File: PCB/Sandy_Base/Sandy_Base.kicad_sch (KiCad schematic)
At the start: 169 parts, among them J1 Conn_02x02_Top_Bottom, J10 Conn_01x03, J2 Conn_02x02_Top_Bottom, J3 Conn_02x02_Top_Bottom, J4 Conn_02x02_Top_Bottom, J5 Conn_02x02_Top_Bottom, J6 Conn_02x02_Top_Bottom, J7 USB_C_Receptacle_USB2.0, J8 Conn_02x03_Odd_Even, J9 Conn_01x02, U1 ATmega32U4-MU, U2 24LC64, Y1 16MHz

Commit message: ひととおりのソケットへの変更完了（プレートまだない）
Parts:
- SW_LSFT1u2: footprint MX_Alps_Hybrid:MXOnly-1U-Hotswap-guide -> MX_Alps_Hybrid:MXOnly-1U-Hotswap-custom5-guide
- SW_LSFT2u1: footprint MX_Alps_Hybrid:MXOnly-2U-Hotswap-ReversedStabilizers-guide2 -> MX_Alps_Hybrid:MXOnly-2U-Hotswap-ReversedStabilizers-guide2-custom11
- SW_RSPC1.5u1: footprint MX_Alps_Hybrid:MXOnly-1.5U-Hotswap-guide -> MX_Alps_Hybrid:MXOnly-1.5U-Hotswap-custom11-guide
- SW_RSPC2u1: footprint MX_Alps_Hybrid:MXOnly-2U-Hotswap-guide2 -> MX_Alps_Hybrid:MXOnly-2U-Hotswap-custom1-guide2
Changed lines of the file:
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@@
       (effects (font (size 1.27 1.27)))
     )
-    (property "Footprint" "MX_Alps_Hybrid:MXOnly-2U-Hotswap-guide2" (at 177.8 172.72 0)
+    (property "Footprint" "MX_Alps_Hybrid:MXOnly-2U-Hotswap-custom1-guide2" (at 177.8 172.72 0)
       (effects (font (size 1.27 1.27)) hide)
     )
@@
       (effects (font (size 1.27 1.27)))
     )
-    (property "Footprint" "MX_Alps_Hybrid:MXOnly-2U-Hotswap-ReversedStabilizers-guide2" (at 29.21 140.97 0)
+    (property "Footprint" "MX_Alps_Hybrid:MXOnly-2U-Hotswap-ReversedStabilizers-guide2-custom11" (at 29.21 140.97 0)
       (effects (font (size 1.27 1.27)) hide)
     )
@@
       (effects (font (size 1.27 1.27)))
     )
-    (property "Footprint" "MX_Alps_Hybrid:MXOnly-1U-Hotswap-guide" (at 45.72 140.97 0)
+    (property "Footprint" "MX_Alps_Hybrid:MXOnly-1U-Hotswap-custom5-guide" (at 45.72 140.97 0)
       (effects (font (size 1.27 1.27)) hide)
     )
@@
       (effects (font (size 1.27 1.27)))
     )
-    (property "Footprint" "MX_Alps_Hybrid:MXOnly-1.5U-Hotswap-guide" (at 177.8 167.64 0)
+    (property "Footprint" "MX_Alps_Hybrid:MXOnly-1.5U-Hotswap-custom11-guide" (at 177.8 167.64 0)
       (effects (font (size 1.27 1.27)) hide)
     )

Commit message: 微調整
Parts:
- LOGO1: footprint Jones.local:Sandy_logo_w60 -> Jones.local:Sandy_logo_w60_new
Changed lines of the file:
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@@
       (effects (font (size 1.27 1.27)) (justify left))
     )
-    (property "Footprint" "Jones.local:Sandy_logo_w60" (at 223.52 211.455 0)
+    (property "Footprint" "Jones.local:Sandy_logo_w60_new" (at 223.52 211.455 0)
       (effects (font (size 1.27 1.27)) hide)
     )

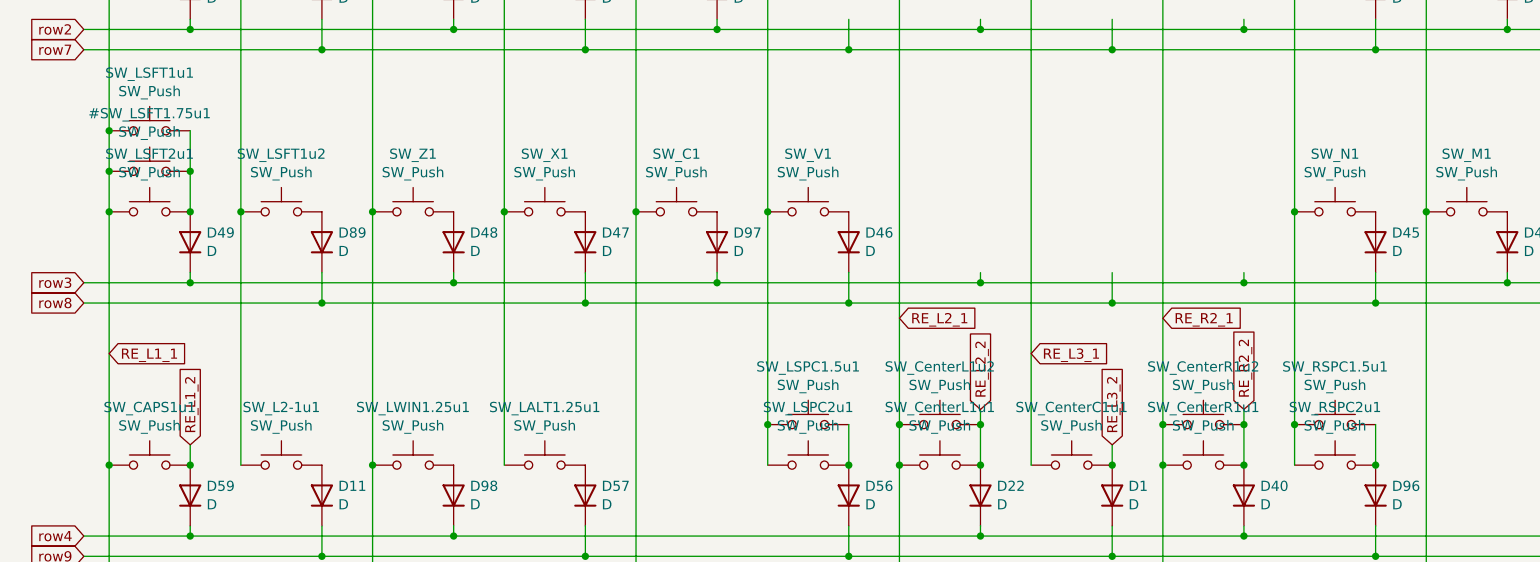
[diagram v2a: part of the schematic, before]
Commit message: 単一レイアウトに変更
最下行：5キー版のみ
左シフト：2uなし、1+1のみ
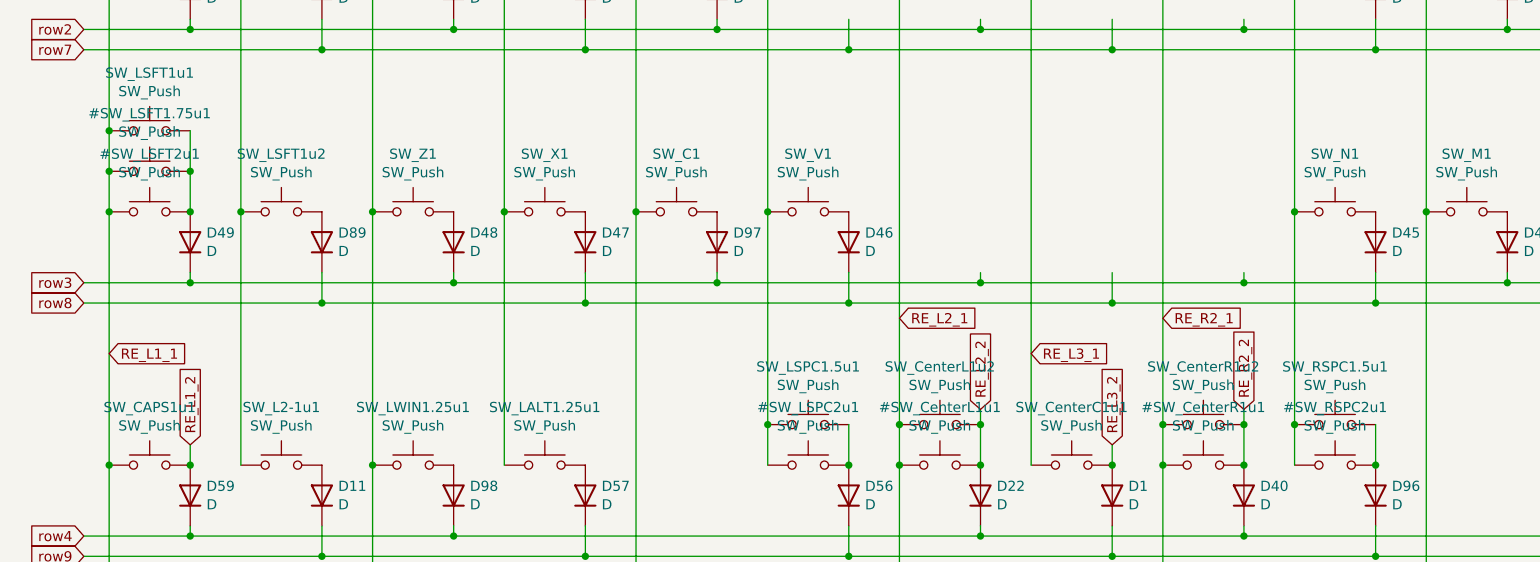
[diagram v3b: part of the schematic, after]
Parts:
- SW_CenterC1u1: footprint MX_Alps_Hybrid:MXOnly-1U-Hotswap-custom4-guide -> MX_Alps_Hybrid:MXOnly-1U-Hotswap-on-RE-guide
- SW_CenterL1u2: footprint MX_Alps_Hybrid:MXOnly-1U-Hotswap-custom2-guide -> MX_Alps_Hybrid:MXOnly-1U-Hotswap-guide
- SW_CenterR1u2: footprint MX_Alps_Hybrid:MXOnly-1U-Hotswap-custom3-guide -> MX_Alps_Hybrid:MXOnly-1U-Hotswap-guide
- SW_LSFT1u2: footprint MX_Alps_Hybrid:MXOnly-1U-Hotswap-custom5-guide -> MX_Alps_Hybrid:MXOnly-1U-Hotswap-guide
- SW_RSPC1.5u1: footprint MX_Alps_Hybrid:MXOnly-1.5U-Hotswap-custom11-guide -> MX_Alps_Hybrid:MXOnly-1.5U-Hotswap-guide
- renumbered SW_CenterL1u1 to #SW_CenterL1u1, SW_CenterR1u1 to #SW_CenterR1u1, SW_LSFT2u1 to #SW_LSFT2u1, SW_LSPC2u1 to #SW_LSPC2u1, SW_RSPC2u1 to #SW_RSPC2u1
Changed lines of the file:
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@@
   (symbol (lib_id "Switch:SW_Push") (at 177.8 177.8 0) (unit 1)
     (in_bom yes) (on_board yes) (dnp no)
-    (property "Reference" "SW_RSPC2u1" (at 177.8 170.561 0)
+    (property "Reference" "#SW_RSPC2u1" (at 177.8 170.561 0)
       (effects (font (size 1.27 1.27)))
     )
@@
       (project "Sandy_Base"
         (path "/a99ab643-cdc7-4f8c-8088-c1f4faa914d1"
-          (reference "SW_RSPC2u1") (unit 1)
+          (reference "#SW_RSPC2u1") (unit 1)
         )
       )
@@
   (symbol (lib_id "Switch:SW_Push") (at 29.21 146.05 0) (unit 1)
     (in_bom yes) (on_board yes) (dnp no)
-    (property "Reference" "SW_LSFT2u1" (at 29.21 138.811 0)
+    (property "Reference" "#SW_LSFT2u1" (at 29.21 138.811 0)
       (effects (font (size 1.27 1.27)))
     )
@@
       (project "Sandy_Base"
         (path "/a99ab643-cdc7-4f8c-8088-c1f4faa914d1"
-          (reference "SW_LSFT2u1") (unit 1)
+          (reference "#SW_LSFT2u1") (unit 1)
         )
       )
@@
   (symbol (lib_id "Switch:SW_Push") (at 111.76 177.8 0) (unit 1)
     (in_bom yes) (on_board yes) (dnp no)
-    (property "Reference" "SW_LSPC2u1" (at 111.76 170.561 0)
+    (property "Reference" "#SW_LSPC2u1" (at 111.76 170.561 0)
       (effects (font (size 1.27 1.27)))
     )
@@
       (project "Sandy_Base"
         (path "/a99ab643-cdc7-4f8c-8088-c1f4faa914d1"
-          (reference "SW_LSPC2u1") (unit 1)
+          (reference "#SW_LSPC2u1") (unit 1)
         )
       )
@@
       (effects (font (size 1.27 1.27)))
     )
-    (property "Footprint" "MX_Alps_Hybrid:MXOnly-1U-Hotswap-custom5-guide" (at 45.72 140.97 0)
+    (property "Footprint" "MX_Alps_Hybrid:MXOnly-1U-Hotswap-guide" (at 45.72 140.97 0)
       (effects (font (size 1.27 1.27)) hide)
     )
@@
   (symbol (lib_id "Switch:SW_Push") (at 128.27 177.8 0) (unit 1)
     (in_bom yes) (on_board yes) (dnp no)
-    (property "Reference" "SW_CenterL1u1" (at 128.27 170.561 0)
+    (property "Reference" "#SW_CenterL1u1" (at 128.27 170.561 0)
       (effects (font (size 1.27 1.27)))
     )
@@
       (project "Sandy_Base"
         (path "/a99ab643-cdc7-4f8c-8088-c1f4faa914d1"
-          (reference "SW_CenterL1u1") (unit 1)
+          (reference "#SW_CenterL1u1") (unit 1)
         )
       )
@@
   (symbol (lib_id "Switch:SW_Push") (at 161.29 177.8 0) (unit 1)
     (in_bom yes) (on_board yes) (dnp no)
-    (property "Reference" "SW_CenterR1u1" (at 161.29 170.561 0)
+    (property "Reference" "#SW_CenterR1u1" (at 161.29 170.561 0)
       (effects (font (size 1.27 1.27)))
     )
@@
       (project "Sandy_Base"
         (path "/a99ab643-cdc7-4f8c-8088-c1f4faa914d1"
-          (reference "SW_CenterR1u1") (unit 1)
+          (reference "#SW_CenterR1u1") (unit 1)
         )
       )
@@
       (effects (font (size 1.27 1.27)))
     )
-    (property "Footprint" "MX_Alps_Hybrid:MXOnly-1U-Hotswap-custom4-guide" (at 144.78 172.72 0)
+    (property "Footprint" "MX_Alps_Hybrid:MXOnly-1U-Hotswap-on-RE-guide" (at 144.78 172.72 0)
       (effects (font (size 1.27 1.27)) hide)
     )
@@
       (effects (font (size 1.27 1.27)))
     )
-    (property "Footprint" "MX_Alps_Hybrid:MXOnly-1U-Hotswap-custom2-guide" (at 128.27 167.64 0)
+    (property "Footprint" "MX_Alps_Hybrid:MXOnly-1U-Hotswap-guide" (at 128.27 167.64 0)
       (effects (font (size 1.27 1.27)) hide)
     )
@@
       (effects (font (size 1.27 1.27)))
     )
-    (property "Footprint" "MX_Alps_Hybrid:MXOnly-1.5U-Hotswap-custom11-guide" (at 177.8 167.64 0)
+    (property "Footprint" "MX_Alps_Hybrid:MXOnly-1.5U-Hotswap-guide" (at 177.8 167.64 0)
       (effects (font (size 1.27 1.27)) hide)
     )
@@
       (effects (font (size 1.27 1.27)))
     )
-    (property "Footprint" "MX_Alps_Hybrid:MXOnly-1U-Hotswap-custom3-guide" (at 161.29 167.64 0)
+    (property "Footprint" "MX_Alps_Hybrid:MXOnly-1U-Hotswap-guide" (at 161.29 167.64 0)
       (effects (font (size 1.27 1.27)) hide)
     )

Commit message: タブそのままで実用OKと判断し、LEDディフューザータブに繋がるネジ穴を削除
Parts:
- removed H90, H91: MountingHole, locallib:MountingHole_2.2mm_M2_No_Cu, symbol Mechanical:MountingHole
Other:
- note removed: "SCREWS to Diffuser"
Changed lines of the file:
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@@
     (effects (font (size 2.54 2.54) (thickness 0.508) bold) (justify left bottom))
   )
-  (text "SCREWS\nto Diffuser" (at 285.115 174.625 0)
-    (effects (font (size 2.54 2.54) (thickness 0.508) bold) (justify left bottom))
-  )
   (text "Virtual Connection" (at 140.335 284.48 0)
     (effects (font (size 1.27 1.27)) (justify left bottom))
@@
     )
   )
-  (symbol (lib_id "Mechanical:MountingHole") (at 292.1 182.88 0) (unit 1)
-    (in_bom yes) (on_board yes) (dnp no)
-    (property "Reference" "H91" (at 294.64 181.7116 0)
-      (effects (font (size 1.27 1.27)) (justify left))
-    )
-    (property "Value" "MountingHole" (at 294.64 184.023 0)
-      (effects (font (size 1.27 1.27)) (justify left))
-    )
-    (property "Footprint" "locallib:MountingHole_2.2mm_M2_No_Cu" (at 292.1 182.88 0)
-      (effects (font (size 1.27 1.27)) hide)
-    )
-    (property "Datasheet" "~" (at 292.1 182.88 0)
-      (effects (font (size 1.27 1.27)) hide)
-    )
-    (instances
-      (project "Sandy_Base"
-        (path "/a99ab643-cdc7-4f8c-8088-c1f4faa914d1"
-          (reference "H91") (unit 1)
-        )
-      )
-    )
-  )
   (symbol (lib_id "power:GND") (at 209.55 283.845 0) (unit 1)
     (in_bom yes) (on_board yes) (dnp no)
@@
         )
       )
-    )
-  )
-  (symbol (lib_id "Mechanical:MountingHole") (at 292.1 177.8 0) (unit 1)
-    (in_bom yes) (on_board yes) (dnp no)
-    (property "Reference" "H90" (at 294.64 176.6316 0)
-      (effects (font (size 1.27 1.27)) (justify left))
-    )
-    (property "Value" "MountingHole" (at 294.64 178.943 0)
-      (effects (font (size 1.27 1.27)) (justify left))
-    )
-    (property "Footprint" "locallib:MountingHole_2.2mm_M2_No_Cu" (at 292.1 177.8 0)
-      (effects (font (size 1.27 1.27)) hide)
-    )
-    (property "Datasheet" "~" (at 292.1 177.8 0)
-      (effects (font (size 1.27 1.27)) hide)
-    )
-    (instances
-      (project "Sandy_Base"
-        (path "/a99ab643-cdc7-4f8c-8088-c1f4faa914d1"
-          (reference "H90") (unit 1)
-        )
-      )

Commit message: 変更：USBコネクタをHRO TYPE-C-31-M-12に変更しSMTAに対応させる
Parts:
- J7: footprint Connector_USB:USB_C_Receptacle_GCT_USB4085 -> Connector_USB:USB_C_Receptacle_HRO_TYPE-C-31-M-12; LCSC (none) -> C165948
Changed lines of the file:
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@@
       (effects (font (size 1.27 1.27)))
     )
-    (property "Footprint" "Connector_USB:USB_C_Receptacle_GCT_USB4085" (at 334.01 167.64 0)
+    (property "Footprint" "Connector_USB:USB_C_Receptacle_HRO_TYPE-C-31-M-12" (at 334.01 167.64 0)
       (effects (font (size 1.27 1.27)) hide)
     )
@@
       (effects (font (size 1.27 1.27)) hide)
     )
+    (property "LCSC" "C165948" (at 330.2 167.64 0)
+      (effects (font (size 1.27 1.27)) hide)
+    )

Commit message: 変更：アクリル板を入れるための、パーツ移動
ダイオード、左端スイッチの上限反転、USBコネクタ周りのパーツを移動
Base基板の外形フットプリントで、右上ネジ穴にNPTHが残っていたのを除去。
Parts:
- D1: renamed from D28; footprint locallib:D_SOD-123_Emphasized_Direction_Line -> locallib:D_SOD-123_Emphasized_Direction_Line_Reference_on_bottom
- D10: renamed from D35; footprint locallib:D_SOD-123_Emphasized_Direction_Line -> locallib:D_SOD-123_Emphasized_Direction_Line_Reference_on_bottom
- D11: renamed from D34; footprint locallib:D_SOD-123_Emphasized_Direction_Line -> locallib:D_SOD-123_Emphasized_Direction_Line_Reference_on_bottom
- D12: renamed from D84; footprint locallib:D_SOD-123_Emphasized_Direction_Line -> locallib:D_SOD-123_Emphasized_Direction_Line_Reference_on_bottom
- D13: renamed from D44; footprint locallib:D_SOD-123_Emphasized_Direction_Line -> locallib:D_SOD-123_Emphasized_Direction_Line_Reference_on_bottom
- D14: renamed from D32; footprint locallib:D_SOD-123_Emphasized_Direction_Line -> locallib:D_SOD-123_Emphasized_Direction_Line_Reference_on_bottom
- D15: renamed from D49; footprint locallib:D_SOD-123_Emphasized_Direction_Line -> locallib:D_SOD-123_Emphasized_Direction_Line_Reference_on_bottom
- D16: renamed from D89; footprint locallib:D_SOD-123_Emphasized_Direction_Line -> locallib:D_SOD-123_Emphasized_Direction_Line_Reference_on_bottom
- D17: renamed from D48; footprint locallib:D_SOD-123_Emphasized_Direction_Line -> locallib:D_SOD-123_Emphasized_Direction_Line_Reference_on_bottom
- D18: renamed from D47; footprint locallib:D_SOD-123_Emphasized_Direction_Line -> locallib:D_SOD-123_Emphasized_Direction_Line_Reference_on_bottom
- D19: renamed from D97; footprint locallib:D_SOD-123_Emphasized_Direction_Line -> locallib:D_SOD-123_Emphasized_Direction_Line_Reference_on_bottom
- D2: renamed from D27; footprint locallib:D_SOD-123_Emphasized_Direction_Line -> locallib:D_SOD-123_Emphasized_Direction_Line_Reference_on_bottom
- D20: renamed from D46; footprint locallib:D_SOD-123_Emphasized_Direction_Line -> locallib:D_SOD-123_Emphasized_Direction_Line_Reference_on_bottom
- D21: renamed from D45; footprint locallib:D_SOD-123_Emphasized_Direction_Line -> locallib:D_SOD-123_Emphasized_Direction_Line_Reference_on_bottom
- D22: renamed from D43; footprint locallib:D_SOD-123_Emphasized_Direction_Line -> locallib:D_SOD-123_Emphasized_Direction_Line_Reference_on_bottom
- D23: renamed from D94; footprint locallib:D_SOD-123_Emphasized_Direction_Line -> locallib:D_SOD-123_Emphasized_Direction_Line_Reference_on_bottom
- D24: renamed from D93; footprint locallib:D_SOD-123_Emphasized_Direction_Line -> locallib:D_SOD-123_Emphasized_Direction_Line_Reference_on_bottom
- D25: renamed from D41; footprint locallib:D_SOD-123_Emphasized_Direction_Line -> locallib:D_SOD-123_Emphasized_Direction_Line_Reference_on_bottom
- D26: renamed from D91; footprint locallib:D_SOD-123_Emphasized_Direction_Line -> locallib:D_SOD-123_Emphasized_Direction_Line_Reference_on_bottom
- D27: renamed from D59; footprint locallib:D_SOD-123_Emphasized_Direction_Line -> locallib:D_SOD-123_Emphasized_Direction_Line_Reference_on_bottom
- D28: renamed from D11; footprint locallib:D_SOD-123_Emphasized_Direction_Line -> locallib:D_SOD-123_Emphasized_Direction_Line_Reference_on_bottom
- D29: renamed from D98; footprint locallib:D_SOD-123_Emphasized_Direction_Line -> locallib:D_SOD-123_Emphasized_Direction_Line_Reference_on_bottom
- D3: renamed from D24; footprint locallib:D_SOD-123_Emphasized_Direction_Line -> locallib:D_SOD-123_Emphasized_Direction_Line_Reference_on_bottom
- D30: renamed from D57; footprint locallib:D_SOD-123_Emphasized_Direction_Line -> locallib:D_SOD-123_Emphasized_Direction_Line_Reference_on_bottom
- D31: renamed from D56; footprint locallib:D_SOD-123_Emphasized_Direction_Line -> locallib:D_SOD-123_Emphasized_Direction_Line_Reference_on_bottom
- D32: renamed from D22; footprint locallib:D_SOD-123_Emphasized_Direction_Line -> locallib:D_SOD-123_Emphasized_Direction_Line_Reference_on_bottom
- D33: renamed from D1; footprint locallib:D_SOD-123_Emphasized_Direction_Line -> locallib:D_SOD-123_Emphasized_Direction_Line_Reference_on_bottom
- D34: renamed from D40; footprint locallib:D_SOD-123_Emphasized_Direction_Line -> locallib:D_SOD-123_Emphasized_Direction_Line_Reference_on_bottom
- D35: renamed from D96; footprint locallib:D_SOD-123_Emphasized_Direction_Line -> locallib:D_SOD-123_Emphasized_Direction_Line_Reference_on_bottom
- D36: renamed from D53; footprint locallib:D_SOD-123_Emphasized_Direction_Line -> locallib:D_SOD-123_Emphasized_Direction_Line_Reference_on_bottom
- D37: renamed from D92; footprint locallib:D_SOD-123_Emphasized_Direction_Line -> locallib:D_SOD-123_Emphasized_Direction_Line_Reference_on_bottom
- D38: renamed from D52; footprint locallib:D_SOD-123_Emphasized_Direction_Line -> locallib:D_SOD-123_Emphasized_Direction_Line_Reference_on_bottom
- D39: renamed from D51; footprint locallib:D_SOD-123_Emphasized_Direction_Line -> locallib:D_SOD-123_Emphasized_Direction_Line_Reference_on_bottom
- D4: renamed from D74; footprint locallib:D_SOD-123_Emphasized_Direction_Line -> locallib:D_SOD-123_Emphasized_Direction_Line_Reference_on_bottom
- D5: renamed from D39; footprint locallib:D_SOD-123_Emphasized_Direction_Line -> locallib:D_SOD-123_Emphasized_Direction_Line_Reference_on_bottom
- D6: renamed from D79; footprint locallib:D_SOD-123_Emphasized_Direction_Line -> locallib:D_SOD-123_Emphasized_Direction_Line_Reference_on_bottom
- D7: renamed from D38; footprint locallib:D_SOD-123_Emphasized_Direction_Line -> locallib:D_SOD-123_Emphasized_Direction_Line_Reference_on_bottom
- D8: renamed from D37; footprint locallib:D_SOD-123_Emphasized_Direction_Line -> locallib:D_SOD-123_Emphasized_Direction_Line_Reference_on_bottom
- D9: renamed from D87; footprint locallib:D_SOD-123_Emphasized_Direction_Line -> locallib:D_SOD-123_Emphasized_Direction_Line_Reference_on_bottom
- renumbered D10 to D99

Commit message: WIP:　アンダーグローLED #98
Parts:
- removed LED3, LED4: SK6812MINI, locallib:LED_SK6812MINI_PLCC4_3.5x3.5mm_P1.75mm_minimal, symbol LED:SK6812MINI
- added L1, L10, L11, L12, L13, L14, L15, L16, L2, L3, L4, L5, L6, L7, L8, L9: SK6812MINI-E, locallib:YS-SK6812MINI-E_middle_hole_with_small_pad, symbol kbd:SK6812MINI-E
- C1: footprint Capacitor_SMD:C_0805_2012Metric_Pad1.18x1.45mm_HandSolder -> locallib:YS-SK6812MINI-E_middle_hole_with_small_pad
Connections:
- net +5V: now also L1.1 (VDD), L10.1 (VDD), L11.1 (VDD), L12.1 (VDD), L13.1 (VDD), L14.1 (VDD), L15.1 (VDD), L16.1 (VDD), L2.1 (VDD), L3.1 (VDD), L4.1 (VDD), L5.1 (VDD), L6.1 (VDD), L7.1 (VDD), L8.1 (VDD), L9.1 (VDD)
- net GND: now also L1.3 (GND), L10.3 (GND), L11.3 (GND), L12.3 (GND), L13.3 (GND), L14.3 (GND), L15.3 (GND), L16.3 (GND), L2.3 (GND), L3.3 (GND), L4.3 (GND), L5.3 (GND), L6.3 (GND), L7.3 (GND), L8.3 (GND), L9.3 (GND)
- net at LED2.1 (DOUT): now also J10.2 (Pin_2), L1.4 (DIN)
- new net: L12.2 (DOUT), L13.4 (DIN)
- new net: L11.2 (DOUT), L12.4 (DIN)
- new net: L15.2 (DOUT), L16.4 (DIN)
- new net: L10.4 (DIN), L9.2 (DOUT)
- new net: L8.2 (DOUT), L9.4 (DIN)
- new net: L10.2 (DOUT), L11.4 (DIN)
- new net: L1.2 (DOUT), L2.4 (DIN)
- new net: L6.2 (DOUT), L7.4 (DIN)
- new net: L5.2 (DOUT), L6.4 (DIN)
- new net: L4.2 (DOUT), L5.4 (DIN)
- new net: L14.2 (DOUT), L15.4 (DIN)
- new net: L2.2 (DOUT), L3.4 (DIN)
- new net: L13.2 (DOUT), L14.4 (DIN)
- new net: L3.2 (DOUT), L4.4 (DIN)
- new net: L7.2 (DOUT), L8.4 (DIN)
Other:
- note removed: "Right side"
- moved on the sheet: J10, LED1, LED2
